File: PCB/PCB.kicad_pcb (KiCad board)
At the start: 4 copper layers, 75 x 75 mm, 113 parts, among them J1 Conn_01x06_Female, J2 5054332681, U1 Hx711, U10 Hx711, U11 Hx711, U12 Hx711, U13 74HC165, U15 LT3042xMSE, U16 74HC165, U2 Hx711, U3 Hx711, U4 Hx711, U5 Hx711, U6 Hx711, U7 Hx711, U8 Hx711, U9 Hx711

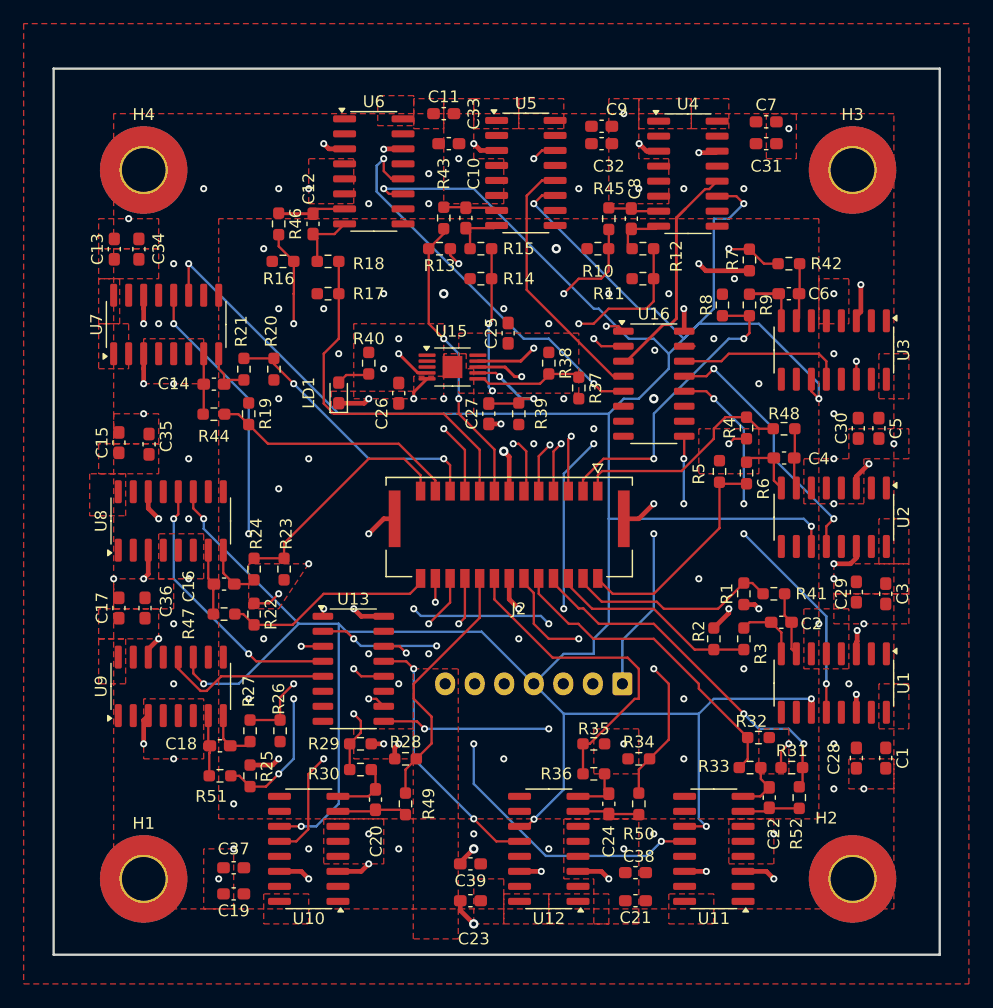
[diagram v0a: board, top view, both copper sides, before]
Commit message: Fixed power lines on the board
Power lines are all now .4 mm unless they are at the linear regulator, in which case they are .25 mm
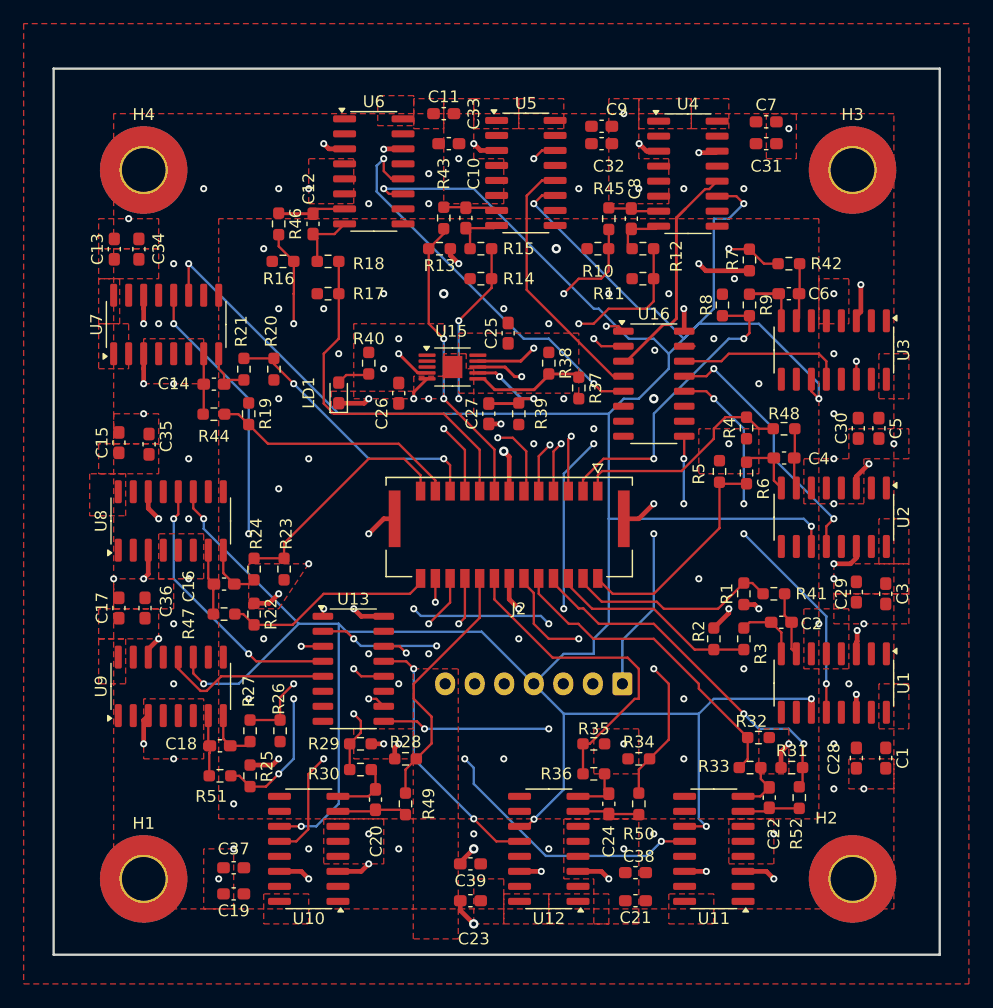
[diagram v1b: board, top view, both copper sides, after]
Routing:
- net /H2N: track 22.3 -> 24.9 mm
- net GND: track 66.8 -> 65.1 mm
- net /DOUT5: track 38.3 -> 37.1 mm
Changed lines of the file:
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@@
 			)
 		)
-		(property ki_fp_filters "Connector*:*_1x??_*")
-		(sheetname "Root")
-		(sheetfile "PCB.kicad_sch")
 		(attr through_hole)
 		(fp_line
@@
 			(layers "*.Cu" "*.Mask")
 			(remove_unused_layers no)
-			(roundrect_rratio 0.1470588235)
+			(roundrect_rratio 0.147059)
 			(net 29 "/S_CLK")
 			(pinfunction "Pin_1")
@@
 		(start 269.8475 141.6325)
 		(end 270.51 140.97)
-		(width 0.2)
+		(width 0.4)
 		(layer "F.Cu")
 		(net 1)
@@
 	)
 	(segment
-		(start 265.8525 115.1475)
-		(end 265.43 115.57)
-		(width 0.2)
-		(layer "F.Cu")
-		(net 1)
-	)
-	(segment
 		(start 215.9 103)
 		(end 215.9 104.14)
@@
 		(start 225.245 129.075)
 		(end 226.525 129.075)
-		(width 0.2)
+		(width 0.4)
 		(layer "F.Cu")
 		(net 1)
@@
 	)
 	(segment
-		(start 266.9275 115.1475)
-		(end 265.8525 115.1475)
-		(width 0.2)
-		(layer "F.Cu")
-		(net 1)
-	)
-	(segment
 		(start 257.81 121.92)
 		(end 259.08 120.65)
@@
 		(start 241.855 99.615)
 		(end 242.57 100.33)
-		(width 0.2)
+		(width 0.4)
 		(layer "F.Cu")
 		(net 1)
@@
 		(start 226.525 129.075)
 		(end 227.33 128.27)
-		(width 0.2)
+		(width 0.4)
 		(layer "F.Cu")
 		(net 1)
@@
 		(start 269.8475 142.98)
 		(end 269.8475 141.6325)
-		(width 0.2)
+		(width 0.4)
 		(layer "F.Cu")
 		(net 1)
@@
 		(start 241.855 99.06)
 		(end 241.855 99.615)
-		(width 0.2)
+		(width 0.4)
 		(layer "F.Cu")
 		(net 1)
@@
 	)
 	(via
-		(at 241.3 111.76)
+		(at 240.03 111.76)
 		(size 0.6)
 		(drill 0.3)
@@
 		(start 248.92 111.76)
 		(end 247.92 111.76)
-		(width 0.2)
+		(width 0.25)
 		(layer "F.Cu")
 		(net 28)
@@
 		(start 245.11 112.1675)
 		(end 247.6 112.1675)
-		(width 0.2)
+		(width 0.25)
 		(layer "F.Cu")
 		(net 28)
@@
 		(start 245.706744 109.575)
 		(end 246.021744 109.89)
-		(width 0.2)
+		(width 0.25)
 		(layer "F.Cu")
 		(net 28)
@@
 		(start 244.1875 109.575)
 		(end 245.706744 109.575)
-		(width 0.2)
+		(width 0.25)
 		(layer "F.Cu")
 		(net 28)
@@
 	)
 	(segment
-		(start 240.03 99.06)
-		(end 240.03 105.41)
+		(start 241.3 111.76)
+		(end 245.59 116.05)
 		(width 0.2)
 		(layer "F.Cu")
@@
 	)
 	(segment
-		(start 242.57 113.03)
-		(end 245.59 116.05)
+		(start 245.59 116.05)
+		(end 245.59 119.58)
 		(width 0.2)
 		(layer "F.Cu")
@@
 	)
 	(segment
-		(start 245.59 116.05)
-		(end 245.59 119.58)
+		(start 240.03 99.06)
+		(end 240.03 105.41)
 		(width 0.2)
 		(layer "F.Cu")
@@
 	)
 	(segment
-		(start 242.57 111.76)
-		(end 242.57 113.03)
-		(width 0.2)
-		(layer "F.Cu")
-		(net 38)
-	)
-	(segment
 		(start 240.03 105.41)
 		(end 241.3 106.68)
@@
 	)
 	(via
-		(at 242.57 111.76)
+		(at 241.3 111.76)
 		(size 0.6)
 		(drill 0.3)
@@
 	)
 	(segment
-		(start 241.3 106.68)
-		(end 242.57 107.95)
-		(width 0.2)
-		(layer "B.Cu")
-		(net 38)
-	)
-	(segment
-		(start 242.57 107.95)
-		(end 242.57 111.76)
+		(start 241.3 111.76)
+		(end 241.3 106.68)
 		(width 0.2)
 		(layer "B.Cu")
@@
 	)
 	(segment
-		(start 247.65 115.57)
-		(end 248.285 116.205)
+		(start 245.872 115.062)
+		(end 247.142 115.062)
 		(width 0.2)
 		(layer "F.Cu")
@@
 	)
 	(segment
-		(start 245.3525 105.1675)
-		(end 245.11 105.41)
+		(start 247.142 115.062)
+		(end 248.285 116.205)
 		(width 0.2)
 		(layer "F.Cu")
@@
 	)
 	(segment
-		(start 245.3525 99.06)
-		(end 245.3525 101.6)
+		(start 242.57 105.156)
+		(end 245.3525 102.3735)
 		(width 0.2)
 		(layer "F.Cu")
@@
 	)
 	(segment
-		(start 247.180003 115.57)
-		(end 247.65 115.57)
+		(start 248.285 116.205)
+		(end 248.285 119.385)
 		(width 0.2)
 		(layer "F.Cu")
@@
 	)
 	(segment
-		(start 245.3525 101.6)
-		(end 245.3525 105.1675)
+		(start 245.3525 99.06)
+		(end 245.3525 101.6)
 		(width 0.2)
 		(layer "F.Cu")
@@
 	)
 	(segment
-		(start 248.285 116.205)
-		(end 248.285 119.385)
+		(start 245.3525 102.3735)
+		(end 245.3525 101.6)
 		(width 0.2)
 		(layer "F.Cu")
@@
 	)
 	(via
-		(at 247.180003 115.57)
+		(at 245.872 115.062)
 		(size 0.6)
 		(drill 0.3)
@@
 	)
 	(via
-		(at 245.421744 111.09)
+		(at 242.57 111.76)
 		(size 0.6)
 		(drill 0.3)
@@
 	)
 	(via
-		(at 245.11 105.41)
+		(at 242.57 105.156)
 		(size 0.6)
 		(drill 0.3)
@@
 	)
 	(segment
-		(start 246.971591 115.361588)
-		(end 246.971591 112.639847)
-		(width 0.2)
-		(layer "In2.Cu")
-		(net 39)
-	)
-	(segment
-		(start 246.971591 112.639847)
-		(end 245.421744 111.09)
-		(width 0.2)
-		(layer "In2.Cu")
-		(net 39)
-	)
-	(segment
-		(start 247.180003 115.57)
-		(end 246.971591 115.361588)
+		(start 245.872 115.062)
+		(end 242.57 111.76)
 		(width 0.2)
 		(layer "In2.Cu")
@@
 	)
 	(segment
-		(start 245.11 110.778256)
-		(end 245.11 105.41)
-		(width 0.2)
-		(layer "B.Cu")
-		(net 39)
-	)
-	(segment
-		(start 245.421744 111.09)
-		(end 245.11 110.778256)
+		(start 242.57 105.156)
+		(end 242.57 111.76)
 		(width 0.2)
 		(layer "B.Cu")
@@
 	(segment
 		(start 244.695 110.075)
-		(end 245.11 110.49)
-		(width 0.2)
+		(end 245.618 110.998)
+		(width 0.25)
 		(layer "F.Cu")
 		(net 46)
 	)
 	(segment
-		(start 249.45 110.49)
+		(start 250.19 109.6625)
+		(end 252.4575 109.6625)
+		(width 0.25)
+		(layer "F.Cu")
+		(net 46)
+	)
+	(segment
+		(start 248.942 110.998)
 		(end 250.19 109.75)
-		(width 0.2)
+		(width 0.25)
 		(layer "F.Cu")
 		(net 46)
 	)
 	(segment
-		(start 250.19 109.6625)
-		(end 252.4575 109.6625)
-		(width 0.2)
+		(start 245.618 110.998)
+		(end 248.942 110.998)
+		(width 0.25)
 		(layer "F.Cu")
 		(net 46)
@@
 	)
 	(segment
-		(start 245.11 110.49)
-		(end 249.45 110.49)
-		(width 0.2)
-		(layer "F.Cu")
-		(net 46)
-	)
-	(segment
 		(start 273.685 135.89)
 		(end 273.685 138.3)
@@
 	)
 	(via
-		(at 243.84 140.97)
+		(at 243.078 142.24)
 		(size 0.6)
 		(drill 0.3)
@@
 	)
 	(segment
-		(start 238.76 135.468529)
-		(end 239.36 134.868529)
+		(start 239.36 134.868529)
+		(end 239.36 134.371471)
 		(width 0.2)
 		(layer "In1.Cu")
@@
 	)
 	(segment
-		(start 239.36 134.868529)
-		(end 239.36 134.371471)
+		(start 239.36 134.371471)
+		(end 238.268529 133.28)
 		(width 0.2)
 		(layer "In1.Cu")
@@
 	)
 	(segment
-		(start 243.84 140.97)
-		(end 241.788529 140.97)
+		(start 243.078 142.24)
+		(end 243.058529 142.24)
 		(width 0.2)
 		(layer "In1.Cu")
@@
 	)
 	(segment
-		(start 241.788529 140.97)
-		(end 238.76 137.941471)
+		(start 238.268529 133.28)
+		(end 238.125 133.28)
 		(width 0.2)
 		(layer "In1.Cu")
@@
 	)
 	(segment
-		(start 238.268529 133.28)
-		(end 238.125 133.28)
+		(start 238.76 135.468529)
+		(end 239.36 134.868529)
 		(width 0.2)
 		(layer "In1.Cu")
@@
 	)
 	(segment
-		(start 239.36 134.371471)
-		(end 238.268529 133.28)
+		(start 243.058529 142.24)
+		(end 238.76 137.941471)
 		(width 0.2)
 		(layer "In1.Cu")
@@
 	)
 	(segment
-		(start 259.715 149.225)
-		(end 258.48 150.46)
+		(start 243.84 144.358529)
+		(end 249.941471 150.46)
 		(width 0.2)
 		(layer "B.Cu")
@@
 	)
 	(segment
-		(start 258.48 150.46)
-		(end 249.941471 150.46)
+		(start 243.84 143.002)
+		(end 243.84 144.358529)
 		(width 0.2)
 		(layer "B.Cu")
@@
 	)
 	(segment
-		(start 243.84 144.358529)
-		(end 243.84 140.97)
+		(start 258.48 150.46)
+		(end 259.715 149.225)
 		(width 0.2)
 		(layer "B.Cu")
@@
 	(segment
 		(start 249.941471 150.46)
-		(end 243.84 144.358529)
+		(end 258.48 150.46)
+		(width 0.2)
+		(layer "B.Cu")
+		(net 100)
+	)
+	(segment
+		(start 243.078 142.24)
+		(end 243.84 143.002)
 		(width 0.2)
 		(layer "B.Cu")

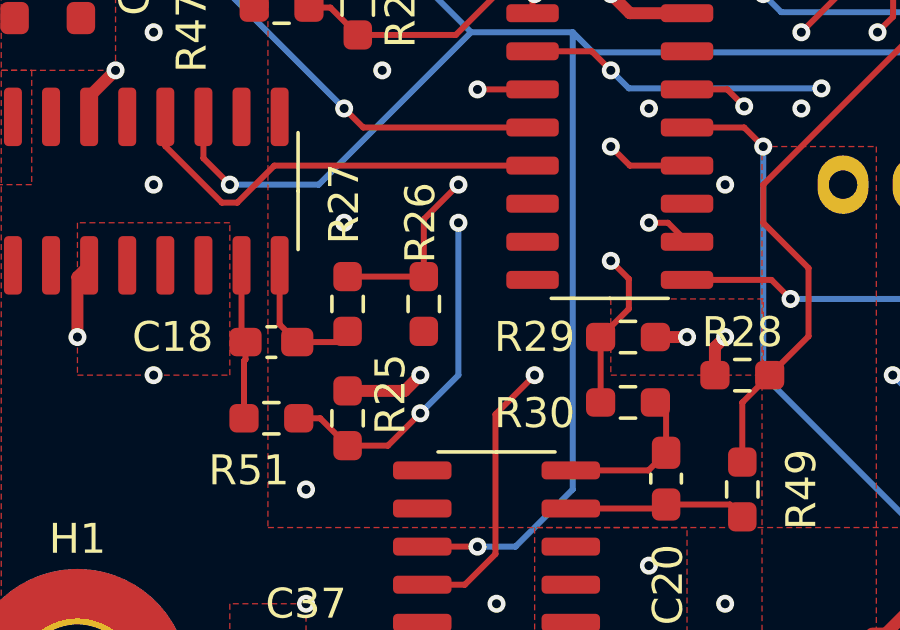
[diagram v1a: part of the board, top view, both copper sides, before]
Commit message: Minor changes to ensure wires are running straigther
Wires adjusted to allow for more direct pathing
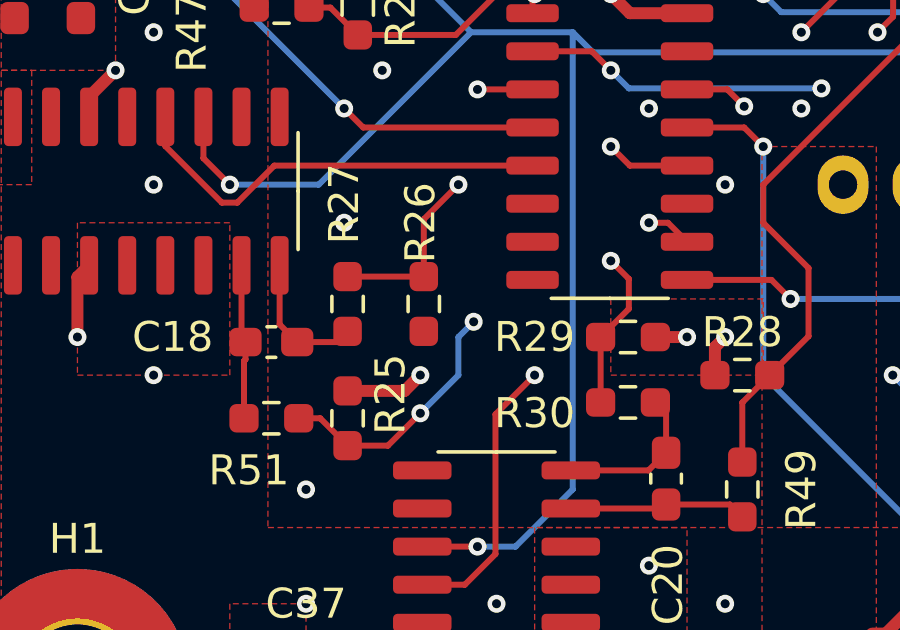
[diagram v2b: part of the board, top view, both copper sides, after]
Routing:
- net /H4P: track 30.4 -> 28.2 mm
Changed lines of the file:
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@@
 	)
 	(segment
-		(start 252.095 114.935)
+		(start 259.158529 107.655)
 		(end 259.158529 107.871471)
 		(width 0.2)
@@
 	(segment
 		(start 259.158529 107.871471)
-		(end 259.158529 107.655)
+		(end 252.095 114.935)
 		(width 0.2)
 		(layer "In1.Cu")
@@
 	)
 	(segment
+		(start 259.158529 107.655)
+		(end 259.158529 107.497942)
+		(width 0.2)
+		(layer "In2.Cu")
+		(net 36)
+	)
+	(segment
 		(start 259.158529 107.497942)
 		(end 265.43 101.226471)
@@
 	)
 	(segment
-		(start 259.158529 107.655)
-		(end 259.158529 107.497942)
-		(width 0.2)
-		(layer "In2.Cu")
-		(net 36)
-	)
-	(segment
 		(start 264.885 104.7375)
 		(end 267.175 104.7375)
@@
 	)
 	(via
-		(at 228.6 137.16)
+		(at 229.108 140.462)
 		(size 0.6)
 		(drill 0.3)
@@
 	)
 	(segment
-		(start 232.41 137.16)
+		(start 229.108 140.462)
 		(end 238.76 130.81)
 		(width 0.2)
@@
 	)
 	(segment
-		(start 228.6 137.16)
-		(end 232.41 137.16)
+		(start 238.76 130.81)
+		(end 240.03 130.81)
 		(width 0.2)
 		(layer "In1.Cu")
@@
 	)
 	(segment
-		(start 238.76 130.81)
-		(end 240.03 130.81)
-		(width 0.2)
-		(layer "In1.Cu")
+		(start 228.6 140.97)
+		(end 228.6 142.24)
+		(width 0.2)
+		(layer "B.Cu")
 		(net 42)
 	)
 	(segment
-		(start 227.33 143.51)
-		(end 228.6 142.24)
+		(start 229.108 140.462)
+		(end 228.6 140.97)
 		(width 0.2)
 		(layer "B.Cu")
@@
 	(segment
 		(start 228.6 142.24)
-		(end 228.6 137.16)
+		(end 227.33 143.51)
 		(width 0.2)
 		(layer "B.Cu")
@@
 	)
 	(segment
+		(start 251.24 115.57)
+		(end 251.24 112.74)
+		(width 0.2)
+		(layer "In2.Cu")
+		(net 118)
+	)
+	(segment
 		(start 251.24 112.74)
 		(end 250.86 112.36)
@@
 		(width 0.2)
 		(layer "In2.Cu")
-		(net 118)
-	)
-	(segment
-		(start 251.24 115.57)
-		(end 251.24 112.74)
-		(width 0.2)
-		(layer "In2.Cu")

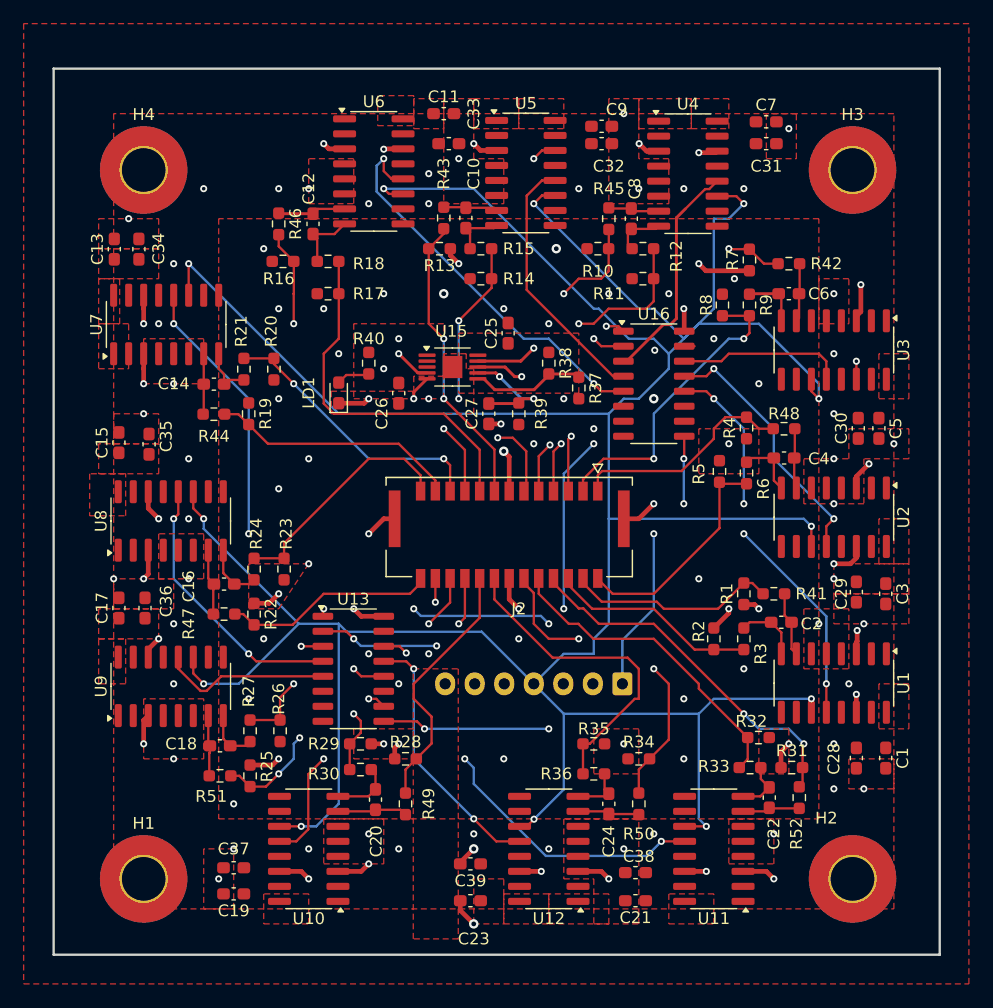
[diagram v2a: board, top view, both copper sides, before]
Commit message: Fixed pour issues
Around the linear regulator, the pour was changed to be a solid fill for the 4.5 Volt zone and the 5V and included the addition of a dozen vias to connect the layers.
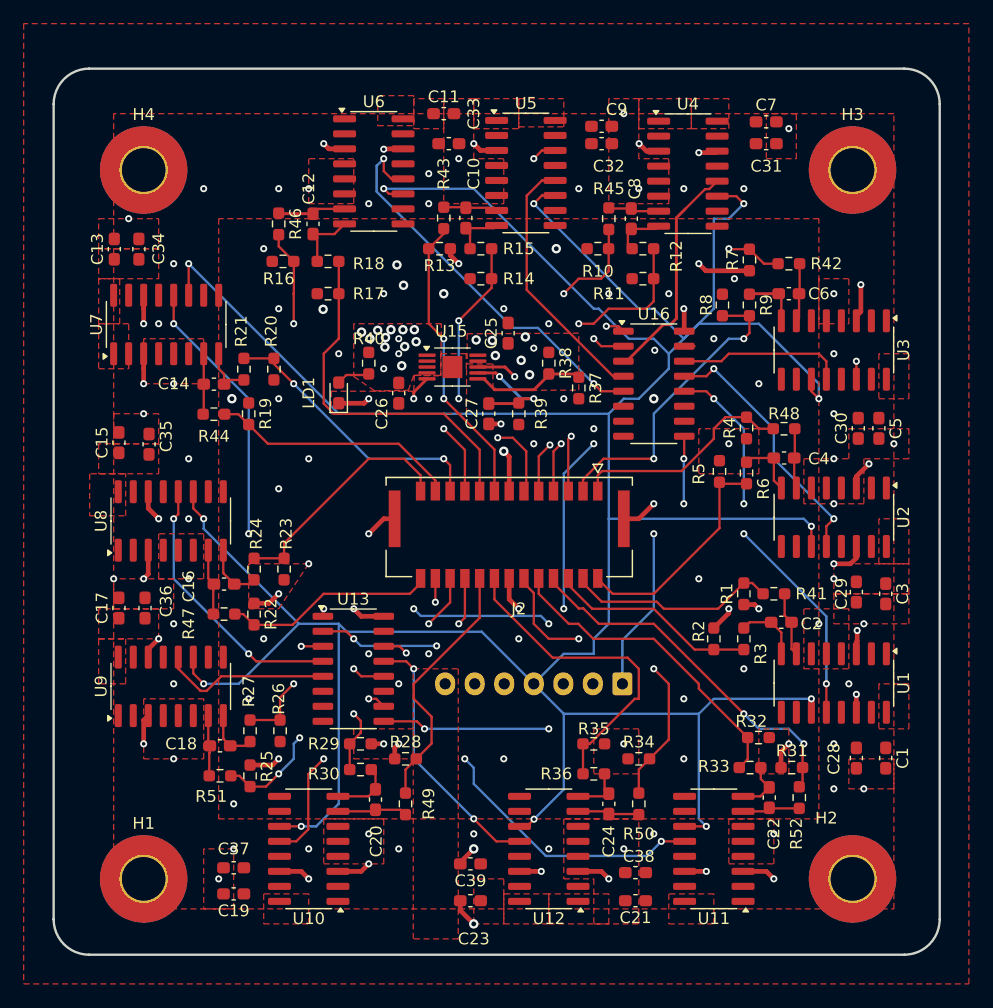
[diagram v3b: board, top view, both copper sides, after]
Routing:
- net 4.5V: track 41.7 -> 36.5 mm, vias 15 -> 21
- net +5V: track 7.86 -> 4.79 mm, vias 32 -> 43
- net GND: track 65.1 -> 64.6 mm, vias 86 -> 89
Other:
- outline, holes or cut-outs redrawn
